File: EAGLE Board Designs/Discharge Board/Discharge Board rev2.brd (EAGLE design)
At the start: 88.2 x 76.7 mm, 27 parts, among them J100 CONNECTOR-5_MICRO_R5S_, J101 CONNECTOR-2_MICROFIT_SMD_RIGH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, K1 RELAY_SPST_NC_POLARIZED_D_24

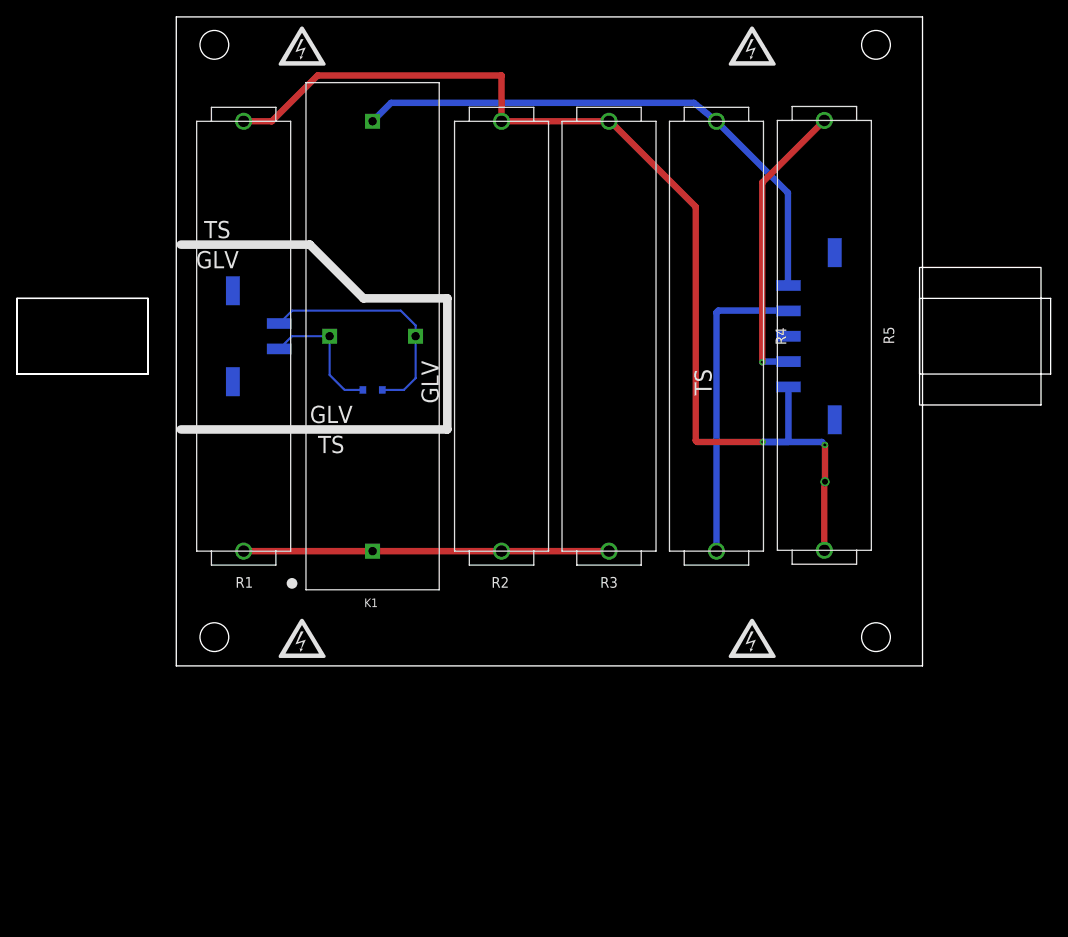
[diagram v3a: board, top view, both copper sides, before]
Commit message: readjusted mounting holes
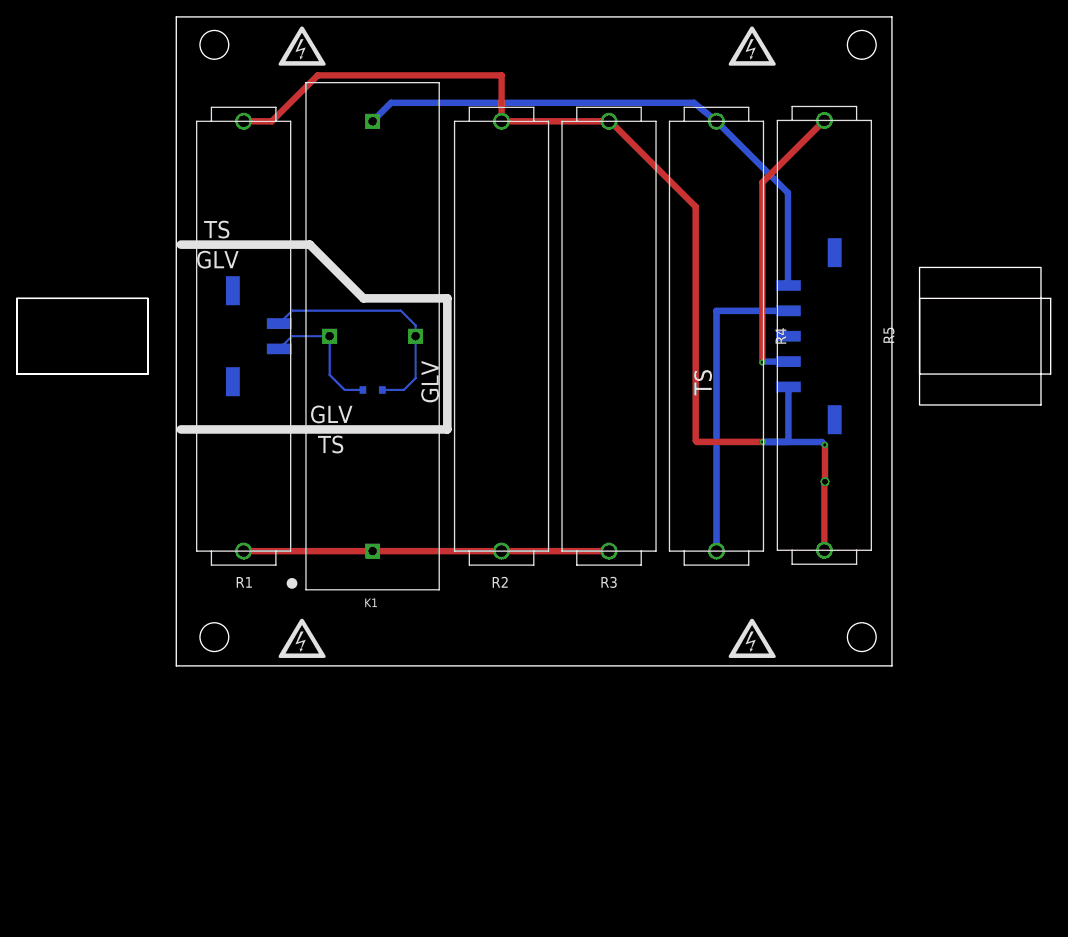
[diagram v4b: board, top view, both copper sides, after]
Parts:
- moved U$16 1.68 mm to (81.0, 3.40)
- moved U$18 1.68 mm to (81.0, 73.4)
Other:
- board size 88.2 x 76.7 mm -> 84.6 x 76.7 mm
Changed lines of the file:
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@@
 <board>
 <plain>
-<wire x1="0" y1="0" x2="88.194" y2="0" width="0" layer="20"/>
-<wire x1="88.194" y1="0" x2="88.194" y2="76.7" width="0" layer="20"/>
-<wire x1="88.194" y1="76.7" x2="0" y2="76.7" width="0" layer="20"/>
+<wire x1="0" y1="0" x2="84.582" y2="0" width="0" layer="20"/>
+<wire x1="84.582" y1="0" x2="84.582" y2="76.7" width="0" layer="20"/>
+<wire x1="84.582" y1="76.7" x2="0" y2="76.7" width="0" layer="20"/>
 <wire x1="0" y1="76.7" x2="0" y2="0" width="0" layer="20"/>
 <wire x1="15.777" y1="49.7884" x2="22.127" y2="43.4384" width="1.016" layer="21"/>
@@
 <element name="U$14" library="HyTechManufacturing" package="HV_MEDIUM" value="" x="14.873" y="3.254" smashed="yes" rot="MR0"/>
 <element name="U$15" library="HyTechManufacturing" package="MOUNTING_M3" value="" x="4.5" y="3.4" smashed="yes"/>
-<element name="U$16" library="HyTechManufacturing" package="MOUNTING_M3" value="" x="82.694" y="3.4" smashed="yes"/>
+<element name="U$16" library="HyTechManufacturing" package="MOUNTING_M3" value="" x="81.0176" y="3.4" smashed="yes"/>
 <element name="U$17" library="HyTechManufacturing" package="MOUNTING_M3" value="" x="4.5" y="73.4" smashed="yes"/>
-<element name="U$18" library="HyTechManufacturing" package="MOUNTING_M3" value="" x="82.694" y="73.4" smashed="yes"/>
+<element name="U$18" library="HyTechManufacturing" package="MOUNTING_M3" value="" x="81.0176" y="73.4" smashed="yes"/>
 <element name="R4" library="HyTechDevices" package="B20-SHORTENED" value="RESISTOR_B20-SHORTENED_15K" x="63.843" y="38.9644" smashed="yes" rot="R270">
 <attribute name="DKPN" value="B20J15KE-ND" x="63.843" y="38.9644" size="1.778" layer="27" rot="R270" display="off"/>
@@
 <contactref element="J100" pad="4"/>
 <contactref element="R4" pad="1"/>
-<wire x1="63.843" y1="13.5644" x2="63.843" y2="41.7704" width="0.762" layer="16"/>
-<wire x1="63.843" y1="41.7704" x2="64.0588" y2="41.9862" width="0.762" layer="16"/>
-<wire x1="64.0588" y1="41.9862" x2="72.3147" y2="41.9862" width="0.762" layer="16"/>
-<wire x1="72.3147" y1="41.9862" x2="72.3393" y2="41.9616" width="0.762" layer="16"/>
+<wire x1="63.843" y1="13.5644" x2="63.843" y2="41.9608" width="0.762" layer="16"/>
+<wire x1="72.3393" y1="41.9616" x2="72.3385" y2="41.9608" width="0.762" layer="16"/>
+<wire x1="72.3385" y1="41.9608" x2="63.843" y2="41.9608" width="0.762" layer="16"/>
 </signal>
 </signals>

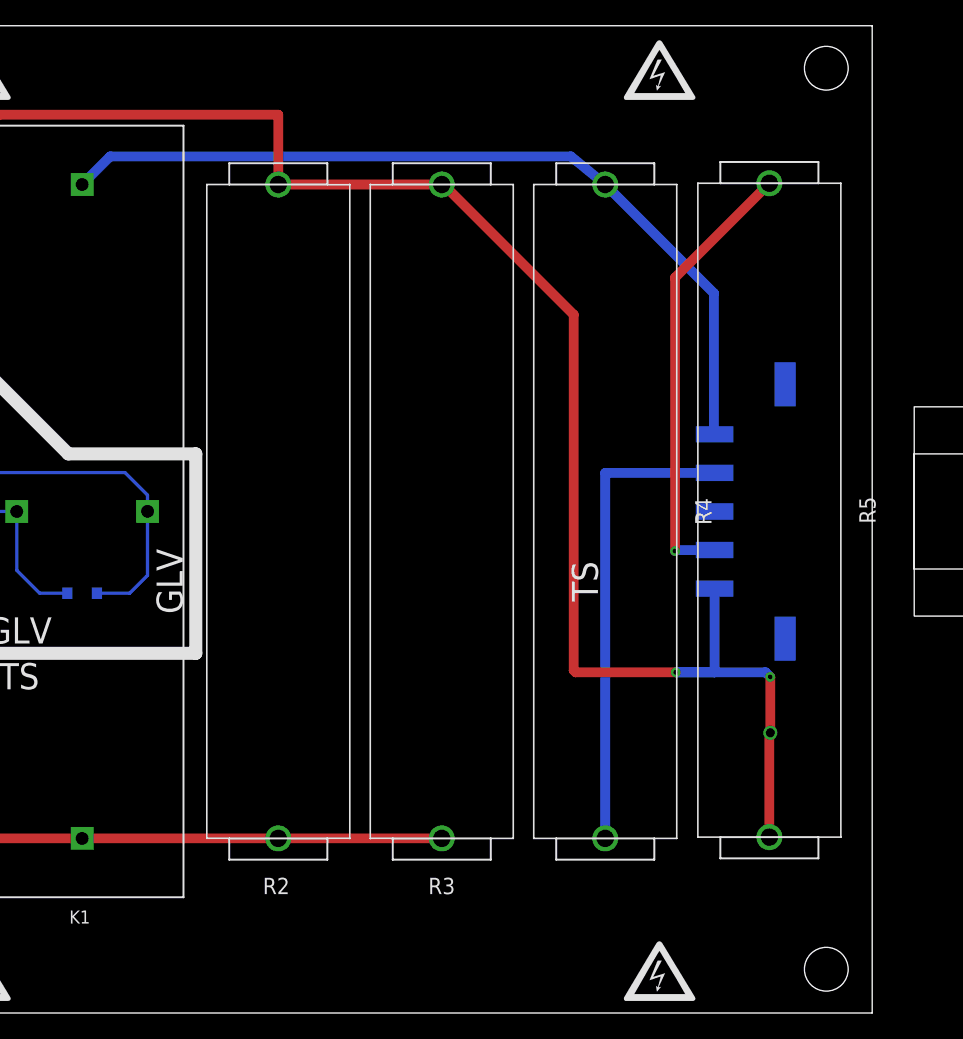
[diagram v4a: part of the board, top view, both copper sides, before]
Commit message: corrected via placement, move TS+,- away from each other, switched up orientation of 2 resistors
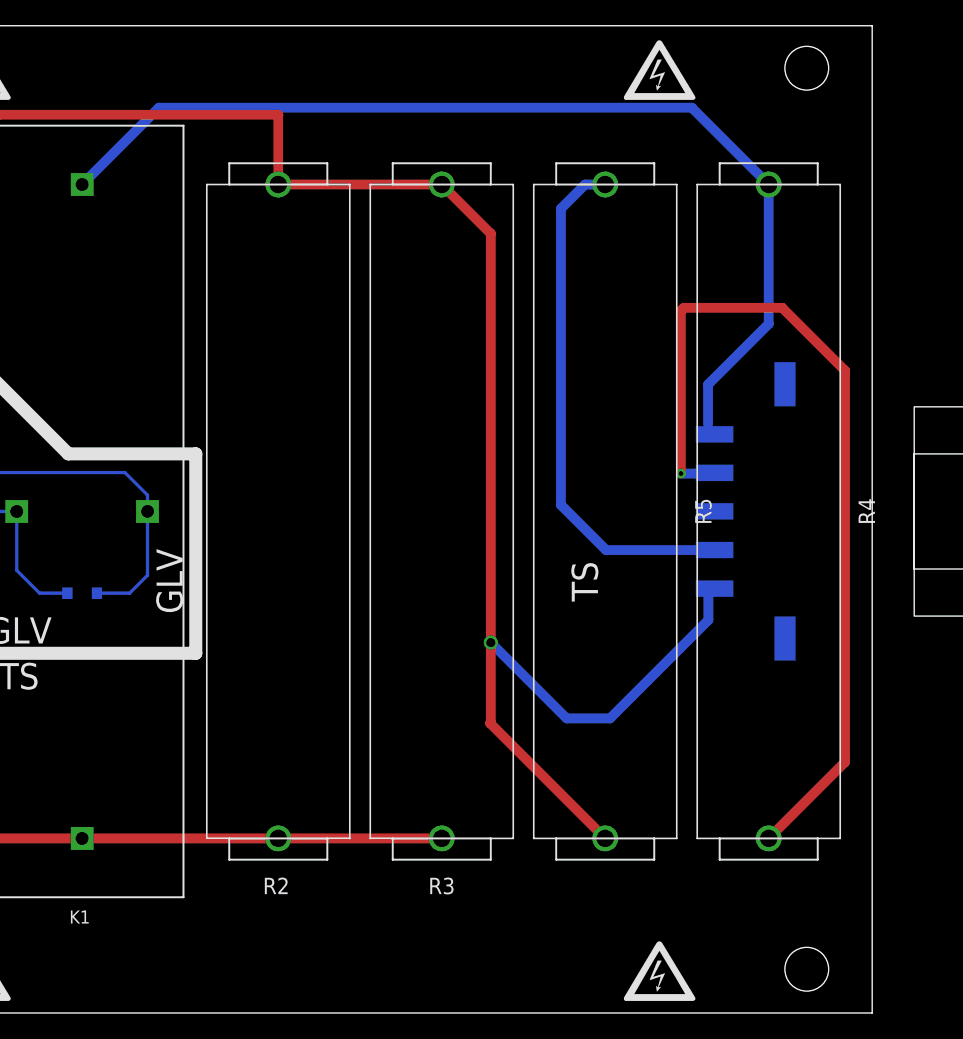
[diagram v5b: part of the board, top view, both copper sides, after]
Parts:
- moved R5 12.8 mm to (63.8, 39.0)
- moved R4 12.7 mm to (76.5, 39.0)
- moved U$16 1.52 mm to (79.5, 3.40)
- moved U$18 1.52 mm to (79.5, 73.4)
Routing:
- net N$2: track 36.9 -> 69.0 mm, vias 0 -> 1
- net TS+UNFUSED: track 65.2 -> 78.9 mm
- net N$1: track 34.7 -> 40.6 mm, vias 1 -> 0
- net TS-UNFUSED: track 131.0 -> 132.3 mm, vias 3 -> 1

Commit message: Update Discharge Board rev2.brd
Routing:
- net N$2: track 69.0 -> 68.0 mm
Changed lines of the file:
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@@
 <contactref element="R4" pad="1"/>
 <wire x1="76.543" y1="13.5644" x2="82.4738" y2="19.4952" width="0.762" layer="1"/>
-<wire x1="77.597" y1="54.7878" x2="69.9516" y2="54.7878" width="0.762" layer="1"/>
-<wire x1="69.9516" y1="54.7878" x2="69.723" y2="54.5592" width="0.762" layer="1"/>
-<wire x1="69.723" y1="54.5592" x2="69.723" y2="41.91" width="0.762" layer="1"/>
+<wire x1="77.597" y1="54.7878" x2="71.501" y2="54.7878" width="0.762" layer="1"/>
+<wire x1="71.501" y1="54.7878" x2="69.723" y2="53.0098" width="0.762" layer="1"/>
+<wire x1="69.723" y1="41.91" x2="69.723" y2="53.0098" width="0.762" layer="1"/>
 <via x="69.723" y="41.91" extent="1-16" drill="0.3556"/>
 <wire x1="69.723" y1="41.91" x2="72.2877" y2="41.91" width="0.762" layer="16"/>
